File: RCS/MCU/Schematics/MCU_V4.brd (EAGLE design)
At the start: 35.2 x 47 mm, 30 parts, among them IC1 FT232RL, J1 MOTOR, J2 POWER, J3 SENSORS, J5 USB-MICROB, Q2 8 MHz, U1 ATMEGA328P_TQFP

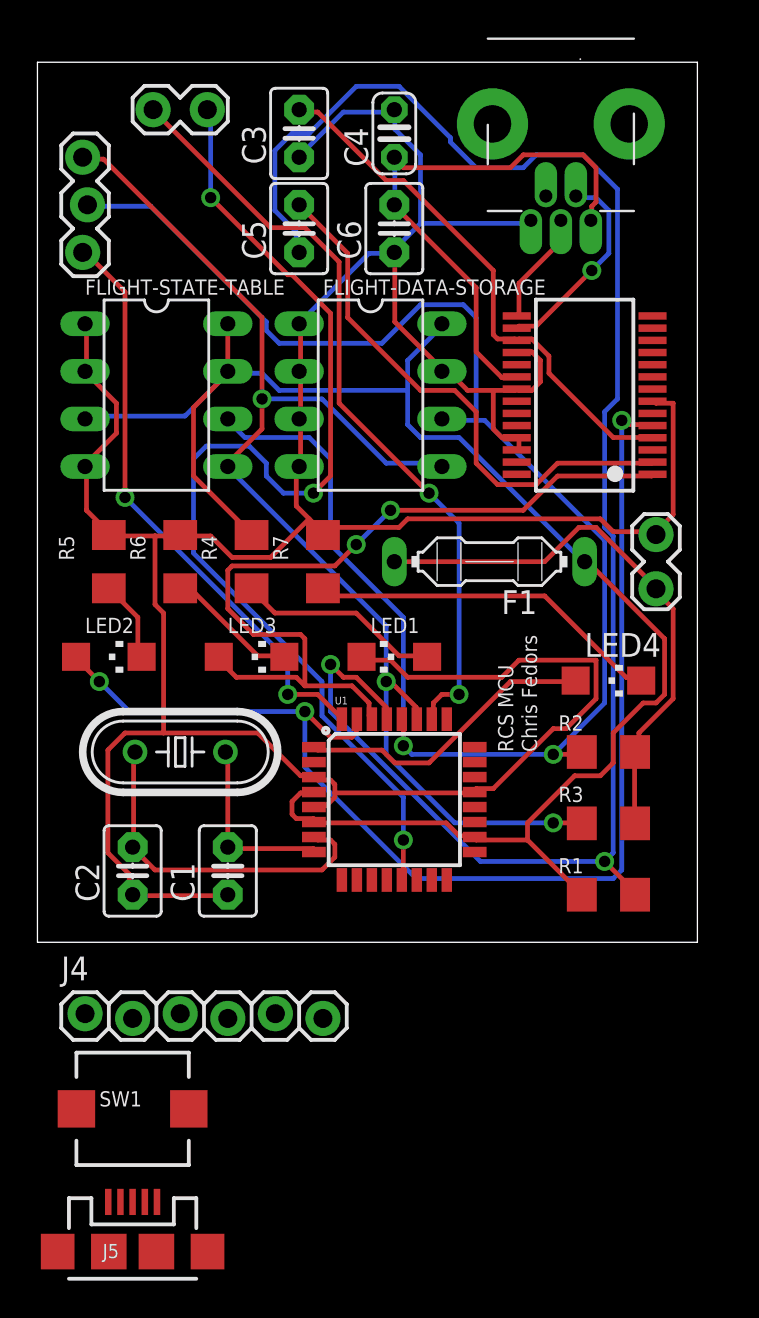
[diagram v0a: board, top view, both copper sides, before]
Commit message: Updated MCU
Added adc, SPI connection, mini USB
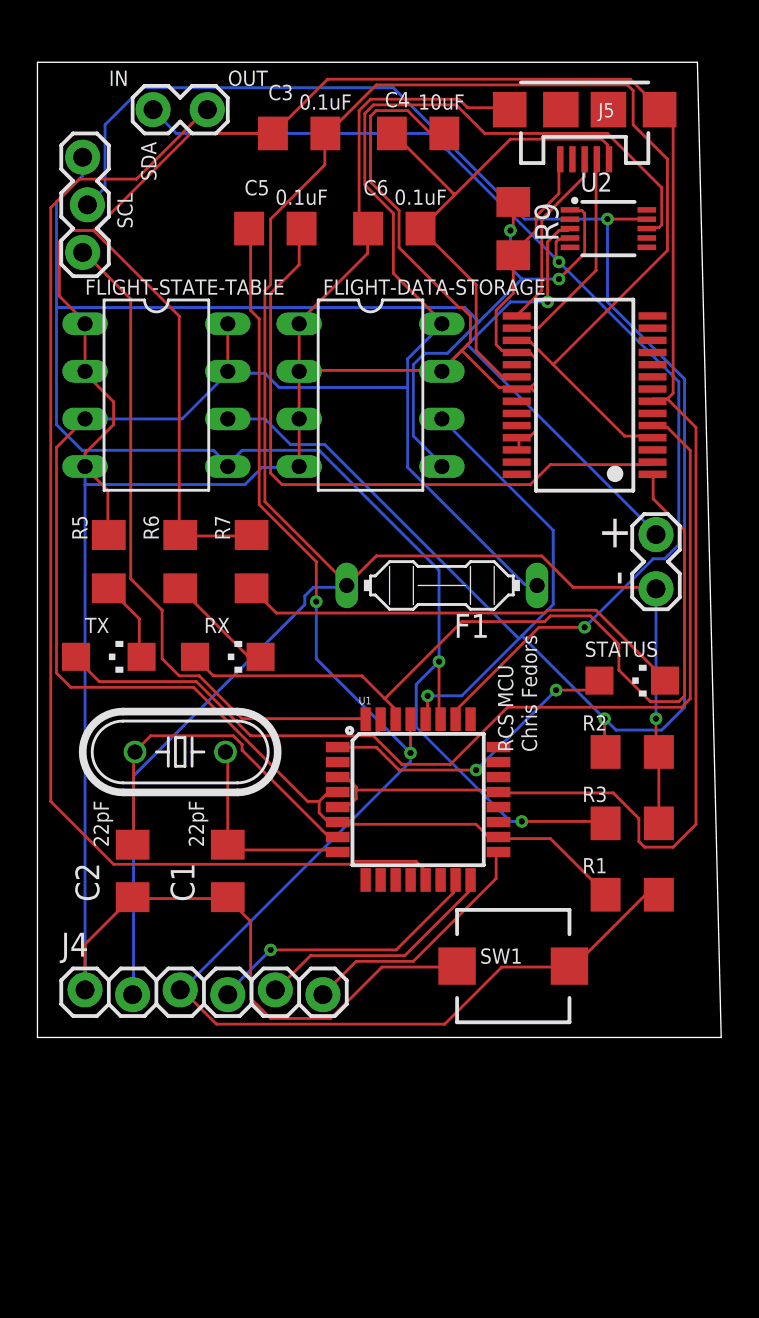
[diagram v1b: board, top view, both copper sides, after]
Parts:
- removed CN1: (no value), adafruit:USB-MINIB-THM-MOLEX
- removed LED1, LED4: Green, adafruit:CHIPLED_1206
- removed LED3: Yellow, adafruit:CHIPLED_1206
- removed R4: 100, adafruit:R1206
- added R9: 10k, adafruit:R1206
- added RX: Yellow, adafruit:CHIPLED_1206
- added STATUS: Green, adafruit:CHIPLED_1206
- added U2: ADS1015, SparkFun-AnalogIC:MSOP10
- C1, C2, C3, C5, C6: device capacitor-wima:C2.5-3 -> eagle-ltspice:C1206
- C4: device adafruit:C025-024X044 -> eagle-ltspice:C1206
- moved J5 65.6 mm to (41.9, 69.8), turned to 180 degrees
- moved SW1 21.7 mm to (38.1, 24.1)
- moved R7 3.81 mm to (24.1, 45.7)
- moved F1 2.84 mm to (34.3, 44.5)
- moved C4 1.27 mm to (33.0, 68.6), turned to 0 degrees
- moved C5 1.27 mm to (25.4, 63.5), turned to 0 degrees
- moved R1 1.27 mm to (44.5, 27.9)
- moved R2 1.27 mm to (44.5, 35.6)
- moved R3 1.27 mm to (44.5, 31.8)
- moved U1 1.27 mm to (33.0, 33.0)
- moved J4 1.27 mm to (15.2, 22.9)
- turned C3 to 0 degrees
- turned C6 to 180 degrees
- renumbered LED2 to TX
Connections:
- removed net N$6: LED1.A, R4.1
- new net SCL: U2.10
- net A4(SDA): now also R9.1, U2.1
- net A5(SCL): now also U2.9
- net DM: no longer CN1.D-
- net DP: no longer CN1.D+
- net FEEDBACK: now also U2.4
- net GND: now also R9.2, U2.3; no longer CN1.GND, LED1.C
- net N$1: now also U2.8; no longer R4.2
- net N$10: now also RX.C; no longer LED3.C
- net N$4: now also STATUS.A; no longer LED4.A
- net N$8: now also STATUS.C; no longer LED4.C
- net RX: now also RX.A; no longer LED3.A
- net USBVDD: no longer CN1.VBUS
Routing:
- net GND: track 183.4 -> 318.8 mm, vias 0 -> 1
- net VDD: track 58.6 -> 130.3 mm, vias 0 -> 1
- net A4(SDA): track 66.6 -> 111.5 mm, vias 3 -> 4
- net N$1: track 90.7 -> 122.8 mm
- net A5(SCL): track 89.2 -> 121.0 mm, vias 2 -> 3
- net FEEDBACK: track 41.5 -> 60.8 mm
- net MOSI: track 0.00 -> 15.1 mm, vias 0 -> 1
- net SCK: track 0.00 -> 13.3 mm
- net MISO: track 0.00 -> 13.2 mm
- net TX: track 65.9 -> 53.5 mm, vias 3 -> 0
- net RESET: track 92.4 -> 80.3 mm
- net N$6: track 10.9 -> 0.00 mm
- net DTR: track 29.2 -> 34.9 mm
- net MOTOR: track 59.0 -> 64.4 mm, vias 3 -> 0
- net N$8: track 19.1 -> 24.3 mm
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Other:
- board size 35.2 x 47 mm -> 36.5 x 52.1 mm
- board text added: "+"
- board text added: "-"
- board text added: "0.1uF"
- board text added: "10uF"
- board text added: "22pF"
- board text added: "IN"
- board text added: "OUT"
- board text added: "SCL"
- board text added: "SDA"
